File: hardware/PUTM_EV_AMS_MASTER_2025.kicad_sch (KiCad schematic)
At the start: 41 parts, among them IC11 ISO6760, IC7 ISO6760, IC8 3.3V/0.5A, J1 M80-5100642, J10 M300-MV10345M1, J12 M80-51034XX, J2 USB_C_Receptacle_USB2.0_14P, J3 M80-51014XX, J4 FTSH-107-01-L-D-K, J5 M80-51004XX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

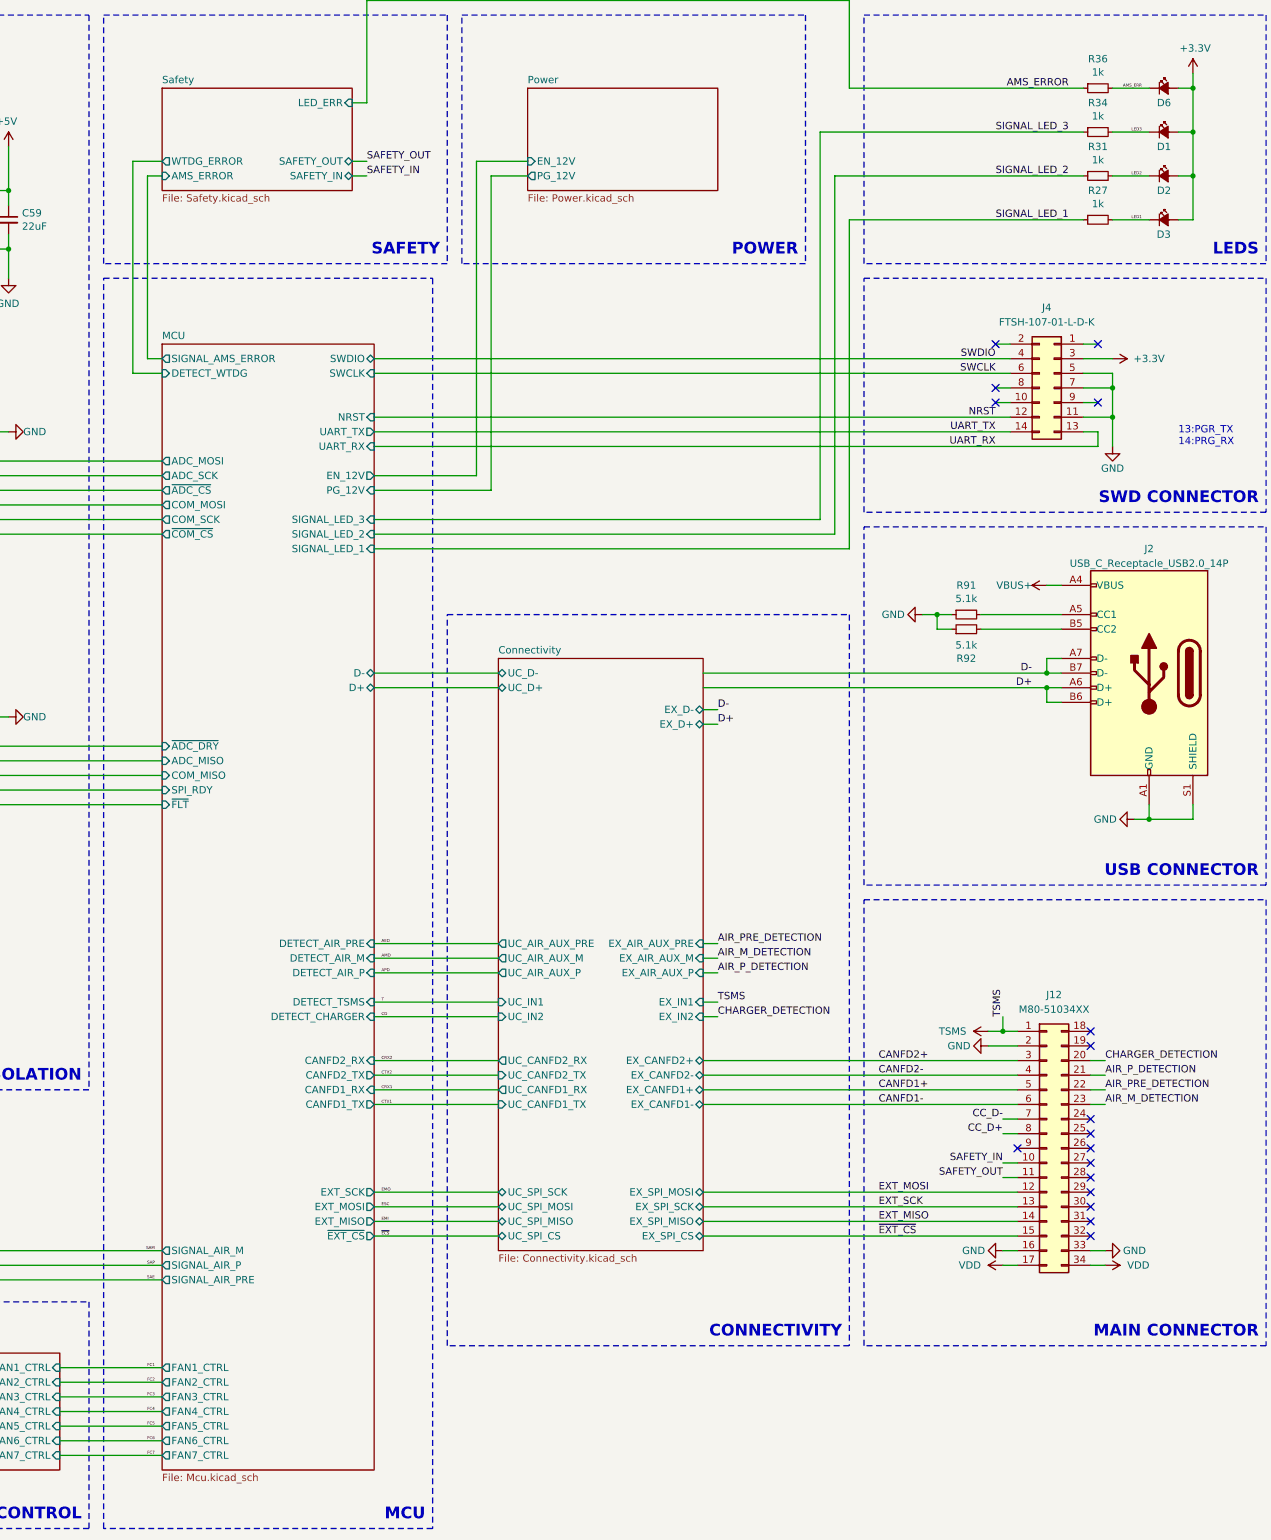
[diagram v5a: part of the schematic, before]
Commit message: sync, layout done, now its time for the routing
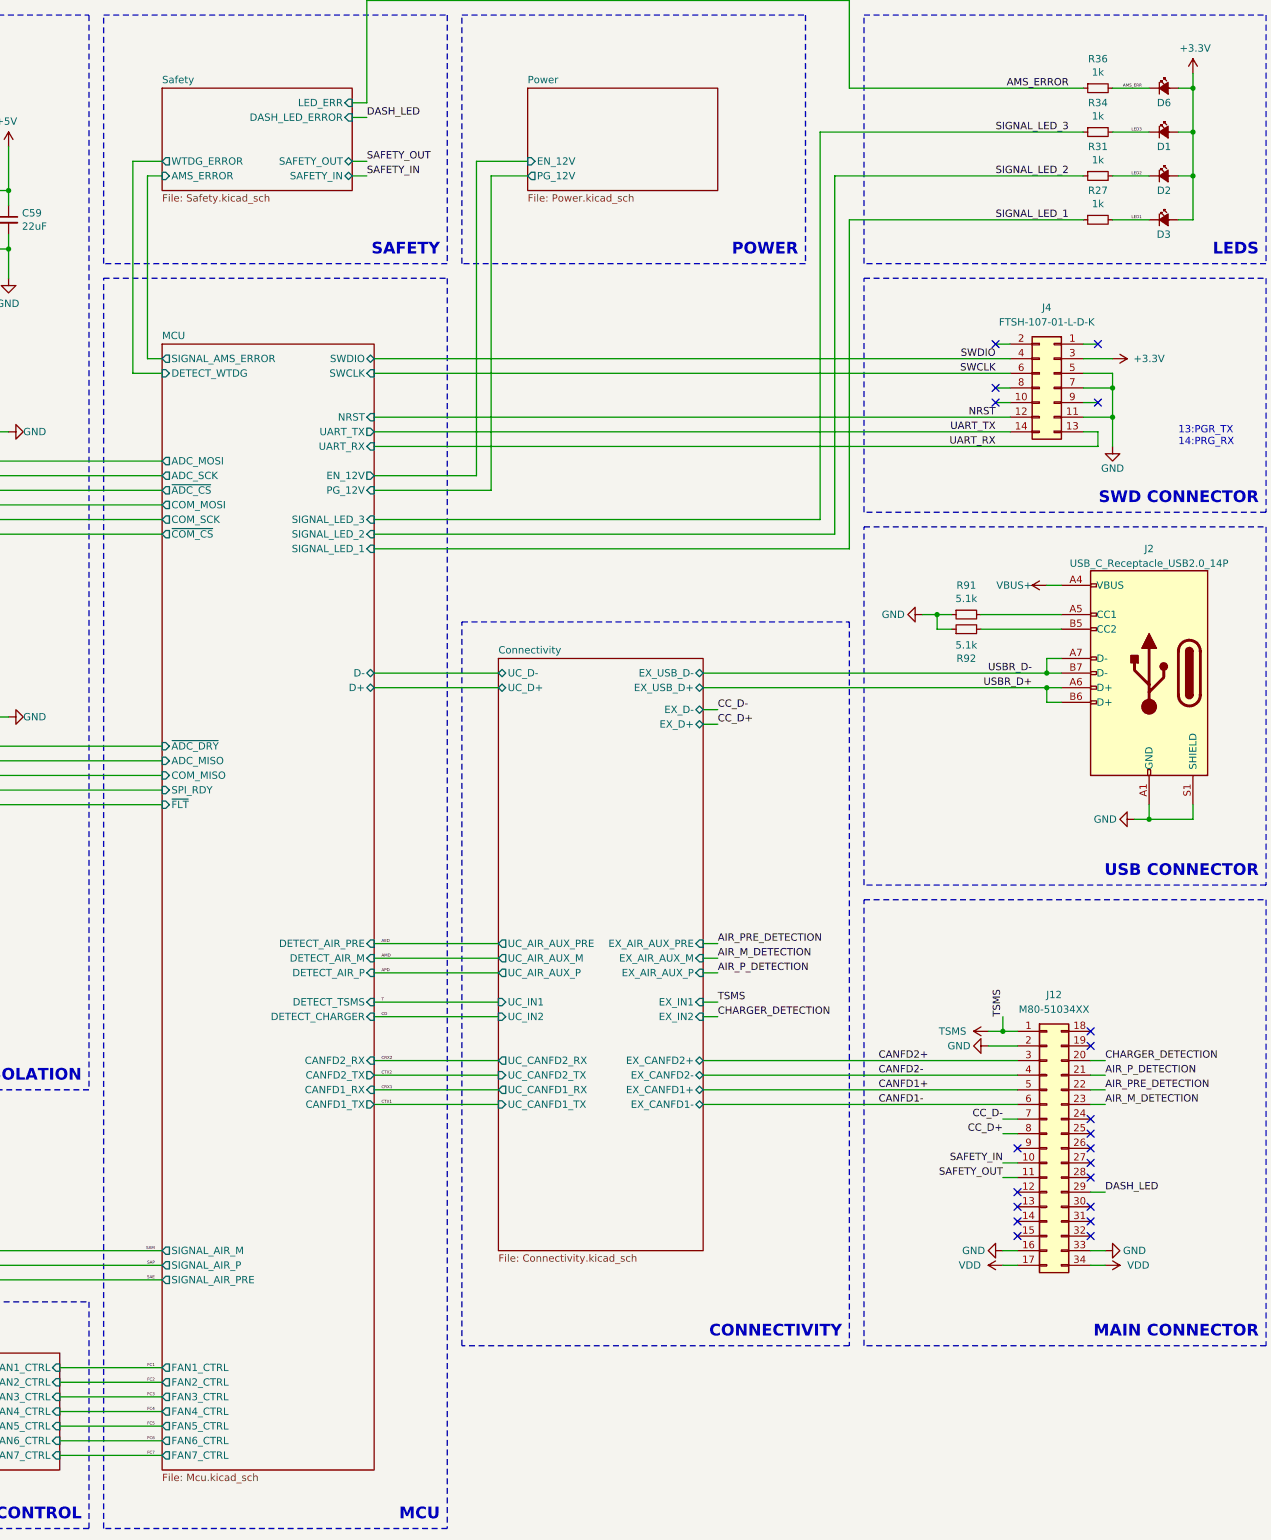
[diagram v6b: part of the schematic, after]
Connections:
- net DASH_LED: now reaches J12.29 (Pin_29)
- net D+ renamed USBR_D+
- net D- renamed USBR_D-
- net EXT_MISO: no longer names the net of J12.14 (Pin_14)
- net EXT_MOSI: no longer names the net of J12.12 (Pin_12)
- net EXT_SCK: no longer names the net of J12.13 (Pin_13)
- net ~{EXT_CS}: no longer names the net of J12.15 (Pin_15)
- no-connect marks 23 -> 26
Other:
- sheet Connectivity ports: added EX_USB_D+, EX_USB_D-; removed EX_SPI_CS, EX_SPI_MISO, EX_SPI_MOSI, EX_SPI_SCK, UC_SPI_CS, UC_SPI_MISO, UC_SPI_MOSI, UC_SPI_SCK
- sheet MCU ports: added none; removed EXT_MISO, EXT_MOSI, EXT_SCK, ~{EXT_CS}
- sheet Safety ports: added DASH_LED_ERROR; removed none

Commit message: this is it i can tell this is the end
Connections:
- net CANFD1+: now also J12.3 (Pin_3); no longer J12.5 (Pin_5)
- net CANFD1-: now also J12.4 (Pin_4); no longer J12.6 (Pin_6)
- net CANFD2+: now also J12.5 (Pin_5); no longer J12.3 (Pin_3)
- net CANFD2-: now also J12.6 (Pin_6); no longer J12.4 (Pin_4)
- net GND: no longer J12.2 (Pin_2)
- no-connect marks 26 -> 27
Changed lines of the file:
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@@
 	)
 	(no_connect
+		(at 361.95 198.12)
+	)
+	(no_connect
 		(at 374.65 231.14)
 	)
@@
 	(wire
 		(pts
-			(xy 356.87 198.12) (xy 361.95 198.12)
-		)
-		(stroke
-			(width 0)
-			(type default)
-		)
-	)
-	(wire
-		(pts
 			(xy 361.95 213.36) (xy 359.41 213.36)
 		)
@@
 	)
 	(label "CRX2"
-		(at 251.46 200.66 0)
+		(at 251.46 205.74 0)
 		(fields_autoplaced yes)
 		(effects
@@
 	)
 	(label "CTX2"
-		(at 251.46 203.2 0)
+		(at 251.46 208.28 0)
 		(fields_autoplaced yes)
 		(effects
@@
 	)
 	(label "CANFD2-"
-		(at 337.82 203.2 0)
+		(at 359.41 208.28 180)
 		(fields_autoplaced yes)
 		(effects
@@
 				(size 1.27 1.27)
 			)
-			(justify left bottom)
+			(justify right bottom)
 		)
 	)
@@
 	)
 	(label "CRX1"
-		(at 251.46 205.74 0)
+		(at 251.46 200.66 0)
 		(fields_autoplaced yes)
 		(effects
@@
 	)
 	(label "CANFD1+"
-		(at 337.82 205.74 0)
+		(at 359.41 200.66 180)
 		(fields_autoplaced yes)
 		(effects
@@
 				(size 1.27 1.27)
 			)
-			(justify left bottom)
+			(justify right bottom)
 		)
 	)
@@
 	)
 	(label "CANFD1-"
-		(at 337.82 208.28 0)
+		(at 359.41 203.2 180)
 		(fields_autoplaced yes)
 		(effects
@@
 				(size 1.27 1.27)
 			)
-			(justify left bottom)
+			(justify right bottom)
 		)
 	)
@@
 	)
 	(label "CTX1"
-		(at 251.46 208.28 0)
+		(at 251.46 203.2 0)
 		(fields_autoplaced yes)
 		(effects
@@
 	)
 	(label "CANFD2+"
-		(at 337.82 200.66 0)
+		(at 359.41 205.74 180)
 		(fields_autoplaced yes)
 		(effects
@@
 				(size 1.27 1.27)
 			)
-			(justify left bottom)
+			(justify right bottom)
 		)
 	)
@@
 	)
 	(symbol
-		(lib_name "GND_5")
-		(lib_id "power:GND")
-		(at 356.87 198.12 270)
-		(unit 1)
-		(exclude_from_sim no)
-		(in_bom yes)
-		(on_board yes)
-		(dnp no)
-		(property "Reference" "#PWR047"
-			(at 350.52 198.12 0)
-			(effects
-				(font
-					(size 1.27 1.27)
-				)
-				(hide yes)
-			)
-		)
-		(property "Value" "GND"
-			(at 351.79 198.12 90)
-			(effects
-				(font
-					(size 1.27 1.27)
-				)
-			)
-		)
-		(property "Footprint" ""
-			(at 356.87 198.12 0)
-			(effects
-				(font
-					(size 1.27 1.27)
-				)
-				(hide yes)
-			)
-		)
-		(property "Datasheet" ""
-			(at 356.87 198.12 0)
-			(effects
-				(font
-					(size 1.27 1.27)
-				)
-				(hide yes)
-			)
-		)
-		(property "Description" ""
-			(at 356.87 198.12 0)
-			(effects
-				(font
-					(size 1.27 1.27)
-				)
-				(hide yes)
-			)
-		)
-		(pin "1"
-		)
-		(instances
-			(project "PUTM_EV_AMS_MASTER_2025"
-				(path "/b456cffc-d9d7-4c91-91f2-36ec9a65dd1b"
-					(reference "#PWR047")
-					(unit 1)
-				)
-			)
-		)
-	)
-	(symbol
 		(lib_id "Device:Polyfuse_Small")
 		(at 85.09 39.37 0)
@@
 		)
 		(pin "CANFD1_RX" input
-			(at 250.19 205.74 0)
+			(at 250.19 200.66 0)
 			(effects
 				(font
@@
 		)
 		(pin "CANFD2_TX" output
-			(at 250.19 203.2 0)
+			(at 250.19 208.28 0)
 			(effects
 				(font
@@
 		)
 		(pin "CANFD2_RX" input
-			(at 250.19 200.66 0)
+			(at 250.19 205.74 0)
 			(effects
 				(font
@@
 		)
 		(pin "CANFD1_TX" output
-			(at 250.19 208.28 0)
+			(at 250.19 203.2 0)
 			(effects
 				(font
@@
 	(sheet
 		(at 271.78 130.81)
-		(size 35.56 102.87)
+		(size 35.56 80.01)
 		(fields_autoplaced yes)
 		(stroke
@@
 		)
 		(property "Sheetfile" "Connectivity.kicad_sch"
-			(at 271.78 234.2646 0)
+			(at 271.78 211.4046 0)
 			(effects
 				(font
@@
 		)
 		(pin "EX_CANFD1-" bidirectional
-			(at 307.34 208.28 0)
+			(at 307.34 203.2 0)
 			(effects
 				(font
@@
 		)
 		(pin "EX_CANFD1+" bidirectional
-			(at 307.34 205.74 0)
+			(at 307.34 200.66 0)
 			(effects
 				(font
@@
 		)
 		(pin "UC_CANFD1_RX" output
-			(at 271.78 205.74 180)
+			(at 271.78 200.66 180)
 			(effects
 				(font
@@
 		)
 		(pin "UC_CANFD1_TX" input
-			(at 271.78 208.28 180)
+			(at 271.78 203.2 180)
 			(effects
 				(font
@@
 		)
 		(pin "EX_CANFD2+" bidirectional
-			(at 307.34 200.66 0)
+			(at 307.34 205.74 0)
 			(effects
 				(font
@@
 		)
 		(pin "EX_CANFD2-" bidirectional
-			(at 307.34 203.2 0)
+			(at 307.34 208.28 0)
 			(effects
 				(font
@@
 		)
 		(pin "UC_CANFD2_TX" input
-			(at 271.78 203.2 180)
+			(at 271.78 208.28 180)
 			(effects
 				(font
@@
 		)
 		(pin "UC_CANFD2_RX" output
-			(at 271.78 200.66 180)
+			(at 271.78 205.74 180)
 			(effects
 				(font

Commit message: bom update
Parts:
- C39, C44, C45, C46, C47, C48, R22, R27, R31, R34, R36, TP4, TP5, TP6, TP7, TP8: Mouser Part Number (none) -> --
- C40, C59, C77: Mouser Part Number (none) -> 810-C2012X5R1V226MAC; Mouser Price/Stock https://www.mouser.pl/ProductDetail/Samsung-Electro-Mechani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 -> (none)
- D1, D2, D3, D6: value SML-D12U1WT86 -> LED; Mouser Part Number (none) -> --
- J1: Mouser Part Number 855-M80-5100642 -> 855-M80-5100622
- J12: Mouser Part Number 855-M80-5103442 -> 855-M80-5103422
- J2: Mouser Part Number (none) -> 656-DX07S0024WJ3R400
- J5, J8: Mouser Part Number 855-M80-5100442 -> 855-M80-5100422
- R91, R92: Mouser Part Number (none) -> 603-RC0603FR-075K1P
- T1: DigiKey Part Number (none) -> 308-2379-1-ND; Mouser Part Number 851-ESMIT-4180/C -> --
